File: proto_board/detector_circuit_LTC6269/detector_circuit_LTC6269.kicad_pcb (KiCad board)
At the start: 4 copper layers, 69.2 x 53.2 mm, 43 parts, among them J1 DET_CONN_PWR, J2 SIPM_CONN, J3 DET_CONN, U12 LTC6269, U13 LTC6269

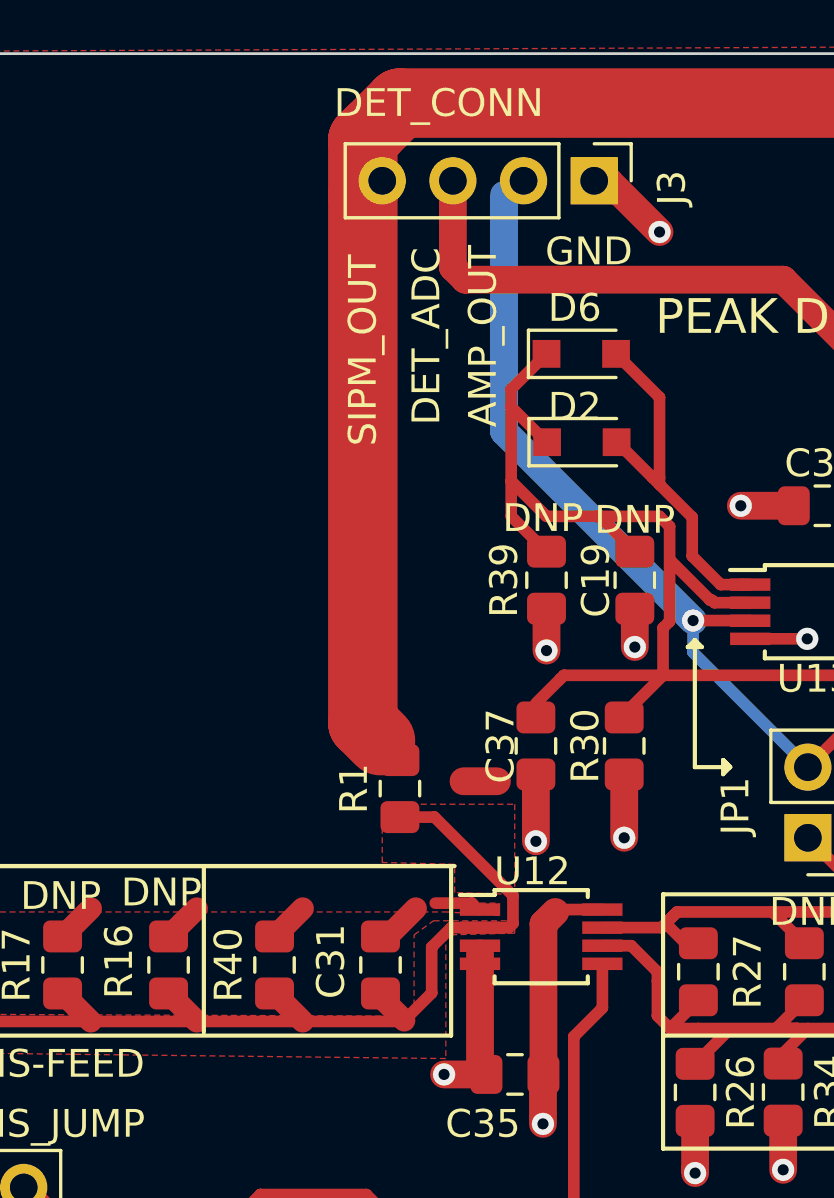
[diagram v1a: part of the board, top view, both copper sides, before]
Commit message: Addressed Zachary's review, re-made gerbers
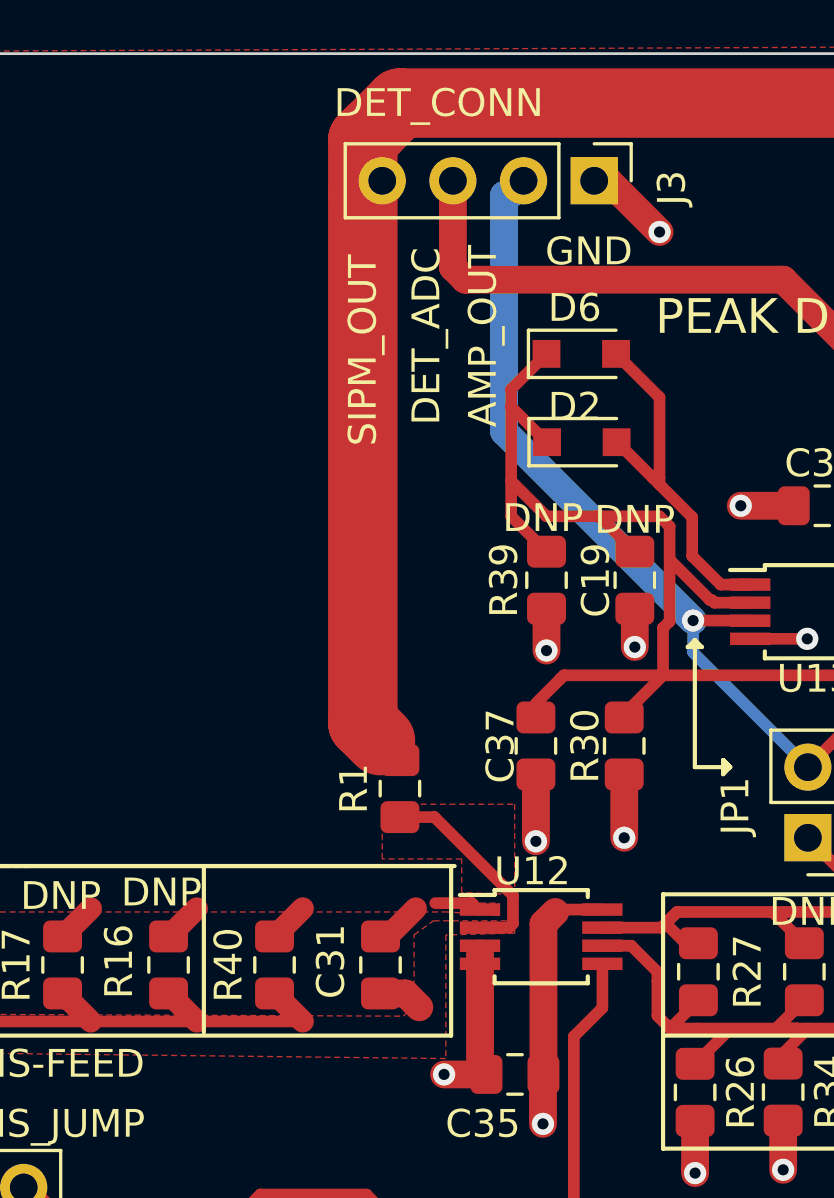
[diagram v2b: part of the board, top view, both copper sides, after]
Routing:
- net Net-(C31-Pad2): track 34.8 -> 26.9 mm
- net (no net): track 1.20 -> 0.00 mm
- net /AMP_OUT: track 38.7 -> 39.7 mm

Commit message: Added dates, fixed some small silkscreen issues generated final gerbers GOOD TO FUCKING GO
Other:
- board text added: "2021-07-15"
